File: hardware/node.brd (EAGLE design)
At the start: 16.5 x 25.6 mm, 48 parts, among them Q1 P-MOSFET, U1 ATMEGA32U4, U2 MCP1703CB/TOREX-XC6206, Y1 8MHz

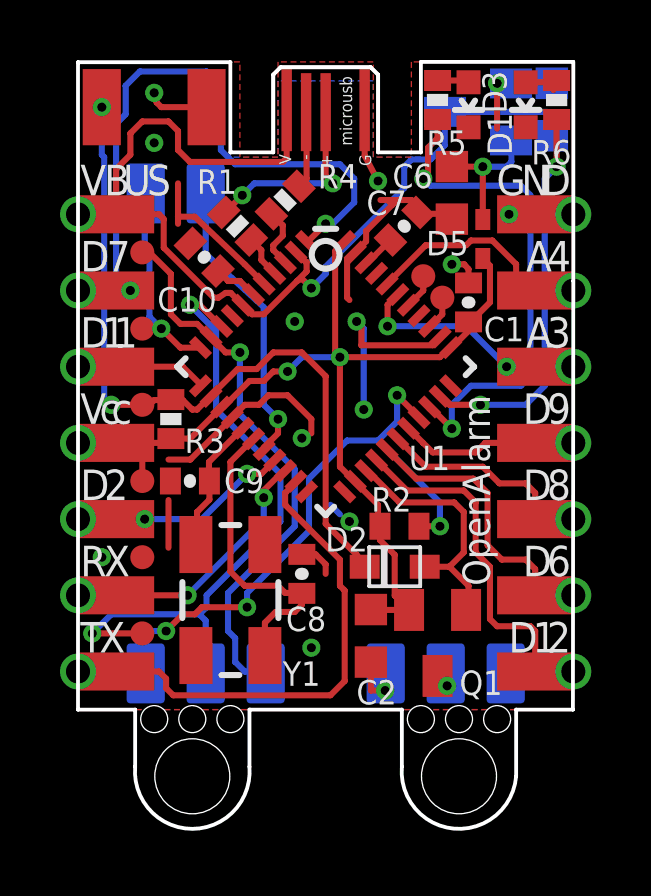
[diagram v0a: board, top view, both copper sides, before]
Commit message: Hardware update
Node 1.0.0, export and node shield
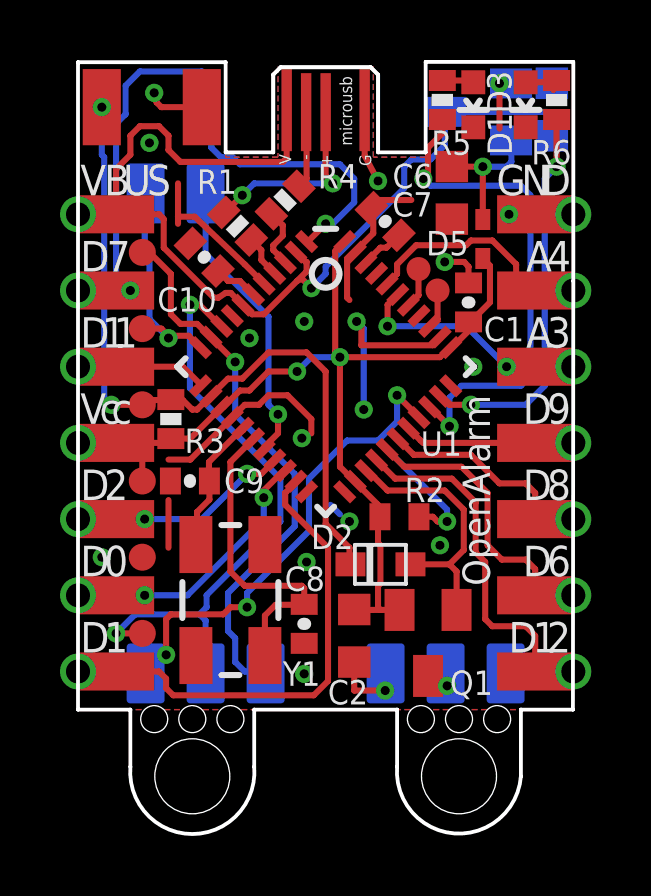
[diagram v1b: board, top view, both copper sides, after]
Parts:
- TP1, TP2, TP3, TP4, TP5, TP6: value TPTP08R -> TPTP09R; device testpad:TP08R -> testpad:TP09R
- moved C8 1.67 mm to (7.54, 2.86), turned to 270 degrees
- moved C7 0.65 mm to (10.2, 16.3), turned to 315 degrees
- moved C2 0.56 mm to (9.21, 2.46)
- moved D2 0.48 mm to (10.1, 4.84)
- moved Q1 0.32 mm to (11.7, 2.22)
- moved R2 0.32 mm to (10.7, 6.43)
- moved TP7 0.29 mm to (11.4, 14.7)
- moved TP8 0.29 mm to (12.0, 14.0)
- moved D3 0.16 mm to (13.2, 20.2)
- moved PAD8 0.16 mm to (4.13, 20.1)
- moved R5 0.16 mm to (12.1, 20.3)
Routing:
- net GND: track 40.2 -> 36.8 mm, vias 14 -> 18
- net SCK: track 21.6 -> 20.0 mm
- net RESET: track 26.1 -> 25.0 mm
- net TXO: track 16.0 -> 15.2 mm
- net VCC: track 32.2 -> 32.7 mm
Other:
- board size 16.5 x 25.6 mm -> 16.5 x 25.7 mm
- board text added: "0"
- board text added: "oa node v 1.x.x"
- board text removed: "R"
- board text removed: "T"
- board text removed: "X"
- board text removed: "oa node v 1.0.0"

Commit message: Before resize
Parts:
- added C3, C4: 1uF, SparkFun:0402-CAP
- added IC1: MAX1555, maxim:SOT23-5L
- added R7, R8: (no value), SparkFun:0402-RES
- added SV1: (no value), con-lsta:FE10
- added TP10, TP9: TPTP08R, testpad:TP08R
- C2: value 100nF -> 1uF; device rcl:C0603K -> SparkFun:0402-CAP
- C5: value 1uF -> 100nF; device rcl:C0603K -> SparkFun:0402-CAP
- C6: value 1u -> 1uF; device rcl:C0603K -> SparkFun:0402-CAP
- moved C5 19.0 mm to (9.53, 2.06), flipped to the top
- moved PAD2 17.3 mm to (15.2, 3.81)
- moved C2 17.1 mm to (1.91, 17.9), turned to 180 degrees
- moved PAD9 14.2 mm to (1.27, 14.0)
- moved PAD3 10.2 mm to (15.2, 11.4)
- moved C6 8.29 mm to (4.21, 17.9), turned to 0 degrees
- moved PAD5 2.54 mm to (15.2, 16.5)
- moved PAD6 2.54 mm to (15.2, 14.0)
- moved PAD13 2.54 mm to (1.27, 3.81)
- moved PAD14 2.54 mm to (1.27, 1.27)
- moved PAD4 2.54 mm to (15.2, 1.27)
- moved PAD10 2.54 mm to (1.27, 11.4)
- moved PAD7 2.54 mm to (1.27, 8.89)
- moved TP8 1.07 mm to (11.2, 14.7)
- moved TP7 0.79 mm to (12.0, 14.2)
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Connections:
- net D10 renamed D10_SEL
- net D13 renamed D13_LED_RED
- net D5 renamed D5_LED_GREEN
- net RXI renamed D0
- net TXO renamed D1
- removed net A0_NOTUSED: TP8.TP, U1.36
- removed net A1_NOTUSED: U1.37
- removed net A5_NOTUSED: U1.41
- removed net D11: PAD7.1, U1.12
- new net A0: PAD6.1, U1.36
- new net A1: PAD5.1, U1.37
- new net A5: TP10.TP, U1.41
- new net D11_IRQ: RFM12B1.IRQ, U1.12
- new net N$28: IC1.3
- new net N$9: C2.2, IC1.1
- net A3: now also TP8.TP; no longer PAD6.1
- net A4: now also R7.1, R8.2; no longer PAD5.1
- net D3: now also PAD7.1; no longer RFM12B1.IRQ
- net GND: now also C2.1, C3.1, C4.1, C5.1, C6.1, IC1.2, R8.1; no longer C2.2, C5.2, C6.2
- net N$11: now also C4.2; no longer C6.1
- net TXLED_NOTUSED: now also TP9.TP
- net VBUS: now also C3.2, R7.2; no longer C5.1
- net VCC: now also C5.2, C6.2, IC1.5; no longer C2.1
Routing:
- net VCC: track 32.7 -> 45.2 mm, vias 2 -> 6
- net A1: track 0.00 -> 7.72 mm, vias 0 -> 2
- net D1: track 15.2 -> 7.73 mm, vias 0 -> 2
- net D11_IRQ: track 0.00 -> 7.39 mm, vias 0 -> 1
- net A4: track 6.93 -> 0.01 mm
- net A3: track 6.68 -> 1.12 mm, vias 2 -> 0
- net VBUS: track 33.9 -> 29.5 mm, vias 1 -> 2
- net A0: track 0.00 -> 4.21 mm, vias 0 -> 2
- net D3: track 9.73 -> 6.26 mm, vias 1 -> 2
- net D11: track 3.10 -> 0.00 mm
- net D0: track 7.92 -> 11.0 mm
- net D6: track 8.49 -> 11.3 mm
- net N$9: track 0.00 -> 2.33 mm, vias 0 -> 1
- net D7: track 21.2 -> 19.1 mm
- net D10_SEL: track 20.5 -> 18.6 mm
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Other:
- board text added: "INT: D0, D1, D2, D3, D7"
- board text added: "PCINT: D8, D9"
- board text removed: "4"

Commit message: New node
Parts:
- moved R8 5.81 mm to (3.73, 18.1), flipped to the top
- moved R7 5.65 mm to (3.73, 17.1), flipped to the top, turned to 180 degrees
- moved SV1 4.84 mm to (35.3, 2.86)
- moved PAD1 2.54 mm to (17.8, 8.89)
- moved PAD11 2.54 mm to (17.8, 6.35)
- moved PAD2 2.54 mm to (17.8, 3.81)
- moved PAD3 2.54 mm to (17.8, 11.4)
- moved PAD4 2.54 mm to (17.8, 1.27)
- moved PAD5 2.54 mm to (17.8, 16.5)
- moved PAD6 2.54 mm to (17.8, 14.0)
- moved C2 2.53 mm to (0.56, 20.1), flipped to the bottom, turned to 270 degrees
- moved C6 2.49 mm to (5.48, 20.1), flipped to the bottom, turned to 270 degrees
- moved R6 2.38 mm to (18.3, 20.3)
- moved C3 2.25 mm to (18.0, 20.3)
- moved D1 2.22 mm to (17.1, 20.2)
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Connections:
- removed net N$9: C2.2, IC1.1
- net VBUS: now also C2.2, IC1.1
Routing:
- net GND: track 35.2 -> 24.7 mm, vias 21 -> 25
- net VBUS: track 29.5 -> 37.0 mm, vias 2 -> 3
- net VCC: track 45.2 -> 50.3 mm, vias 6 -> 4
- net N$9: track 2.33 -> 0.00 mm, vias 1 -> 0
- net A4: track 0.01 -> 2.21 mm
- net D6: track 11.3 -> 12.6 mm
- net A1: track 7.72 -> 9.01 mm
- net D9: track 4.43 -> 5.70 mm
- net D7: track 19.1 -> 20.4 mm
- net D3: track 6.26 -> 7.53 mm
- net D2: track 6.11 -> 7.38 mm
- net D1: track 7.73 -> 9.00 mm
- net A0: track 4.21 -> 5.48 mm
- net D8: track 6.34 -> 7.61 mm
- net RESET: track 26.0 -> 27.2 mm
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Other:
- board size 16.5 x 25.7 mm -> 19.1 x 25.7 mm

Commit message: Node
Avancement
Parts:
- added PAD17, PAD18, PAD19, PAD20, PAD21, PAD22, PAD23, PAD24, PAD25, PAD26, PAD27, PAD28, PAD29, PAD30, PAD31, PAD32, PAD33, PAD34, PAD35, PAD36, PAD37, PAD38, PAD39, PAD40, PAD41, PAD42, PAD43, PAD44, PAD45, PAD46, PAD47, PAD48, PAD49, PAD50, PAD51, PAD52, PAD53, PAD54, PAD55, PAD56, PAD57, PAD58: (no value), wirepad:SMD1,27-2,54
- added TP11: TPTP08R, testpad:TP08R
- moved SV1 21.5 mm to (29.8, 23.7)
- moved R3 0.78 mm to (4.13, 9.76)
- moved C10 0.50 mm to (5.56, 15.0)
- moved R1 0.50 mm to (6.91, 16.2)
- moved C1 0.32 mm to (14.8, 13.7)
- moved C4 0.32 mm to (14.2, 17.3)
- moved C5 0.32 mm to (11.1, 2.06)
- moved C7 0.32 mm to (11.5, 16.5)
- moved D3 0.32 mm to (15.2, 20.2)
- moved D5 0.32 mm to (15.9, 16.4)
- moved Q1 0.32 mm to (13.3, 2.22)
- moved TP10 0.32 mm to (12.8, 15.6)
- moved TP8 0.32 mm to (12.8, 14.7)
- moved IC1 0.32 mm to (3.33, 20.0)
- moved C6 0.32 mm to (5.79, 20.1)
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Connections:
- net TXLED_NOTUSED renamed TXLED
- removed net RXLED_NOTUSED: U1.8
- new net N$13: PAD33.1, PAD34.1
- new net N$27: PAD35.1, PAD36.1
- new net N$29: PAD37.1, PAD38.1
- new net N$30: PAD39.1, PAD40.1
- new net N$31: PAD41.1, PAD42.1
- new net N$32: PAD43.1, PAD44.1
- new net N$40: PAD45.1, PAD46.1
- new net N$41: PAD47.1, PAD48.1
- new net N$42: PAD49.1, PAD50.1
- new net N$43: PAD51.1, PAD52.1
- new net N$44: PAD53.1, PAD54.1
- new net N$45: PAD55.1, PAD56.1
- new net N$46: PAD57.1, PAD58.1
- new net N$9: PAD31.1, PAD32.1
- new net RXLED: TP11.TP, U1.8
- net A0: now also PAD29.1
- net A1: now also PAD30.1
- net D0: now also PAD23.1
- net D1: now also PAD22.1
- net D12: now also PAD28.1
- net D2: now also PAD21.1
- net D3: now also PAD20.1
- net D6: now also PAD24.1
- net D7: now also PAD25.1
- net D8: now also PAD26.1
- net D9: now also PAD27.1
- net GND: now also PAD18.1
- net VBUS: now also PAD17.1
- net VCC: now also PAD19.1
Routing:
- net GND: track 24.7 -> 80.1 mm, vias 25 -> 24
- net A4: track 2.21 -> 15.5 mm, vias 0 -> 2
- net VCC: track 50.3 -> 46.1 mm, vias 4 -> 2
- net D5_LED_GREEN: track 17.0 -> 13.2 mm
- net RXLED: track 0.00 -> 2.19 mm
- net D7: track 20.4 -> 19.6 mm
- net MOSI: track 19.9 -> 20.7 mm
- net D6: track 12.6 -> 13.2 mm
- net D+: track 6.94 -> 7.45 mm
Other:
- board size 19.1 x 25.7 mm -> 39.5 x 25.7 mm
- board text removed: "INT: D0, D1, D2, D3, D7"
- board text removed: "PCINT: D8, D9"

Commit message: Node
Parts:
- removed SV1: (no value), con-lsta:FE10
- added TP12: TPTP08R, testpad:TP08R
- D5: value (none) -> RB751S40
- moved C1 0.65 mm to (15.4, 13.6)
- moved R7 0.40 mm to (4.05, 16.7)
- moved R8 0.32 mm to (4.05, 17.8)
- moved TP7 0.29 mm to (13.7, 14.4)
- moved R4 0.29 mm to (8.65, 16.7)
- moved D5 0.18 mm to (15.7, 16.5)
- moved TP11 0.18 mm to (4.84, 13.6)
- moved PAD31 0.16 mm to (21.3, 16.5)
- moved PAD32 0.16 mm to (21.3, 16.5)
- moved PAD33 0.16 mm to (21.3, 14.0)
- moved PAD34 0.16 mm to (21.3, 14.0)
- moved PAD35 0.16 mm to (21.3, 11.4)
- moved PAD36 0.16 mm to (21.3, 11.4)
- moved PAD37 0.16 mm to (21.3, 8.89)
- moved PAD38 0.16 mm to (21.3, 8.89)
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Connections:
- net VBUS renamed VIN
- removed net N$28: IC1.3
- new net CHG: IC1.3, TP12.TP, U1.33
- net GND: no longer U1.33
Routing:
- net CHG: track 0.00 -> 21.4 mm, vias 0 -> 3
- net GND: track 80.1 -> 68.7 mm, vias 24 -> 25
- net VCC: track 46.1 -> 51.3 mm, vias 2 -> 3
- net A4: track 15.5 -> 13.8 mm
- net D7: track 19.6 -> 18.1 mm, vias 2 -> 1
- net D0: track 11.6 -> 12.7 mm, vias 2 -> 1
- net VIN: track 36.6 -> 35.7 mm
- net D12: track 10.5 -> 11.4 mm, vias 2 -> 1
- net RESET: track 27.1 -> 27.6 mm
- net D3: track 7.84 -> 8.32 mm, vias 2 -> 1
- net D+: track 7.45 -> 7.82 mm, vias 2 -> 0
- net A0: track 5.48 -> 5.69 mm, vias 2 -> 1
- net D13_LED_RED: track 13.6 -> 13.8 mm, vias 2 -> 4
- net A1: track 9.01 -> 8.92 mm, vias 2 -> 1
- net D2: vias 2 -> 1
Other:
- board size 39.5 x 25.7 mm -> 39.4 x 25.7 mm
- board text added: "C"
- board text added: "I"
- board text removed: "B"
- board text removed: "S"
- board text removed: "U"
- board text removed: "c"

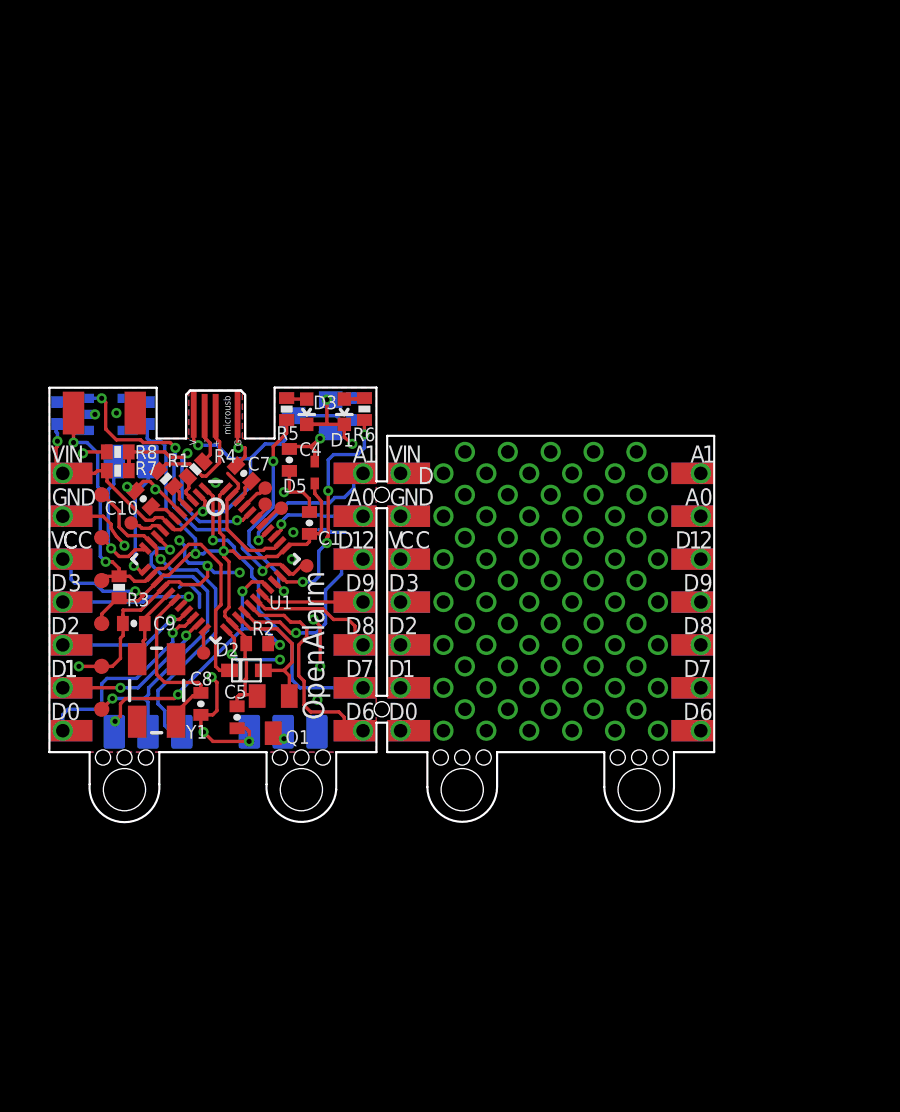
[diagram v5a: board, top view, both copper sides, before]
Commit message: Max1555 backup
Finally, design with max1555 is a bad idea !
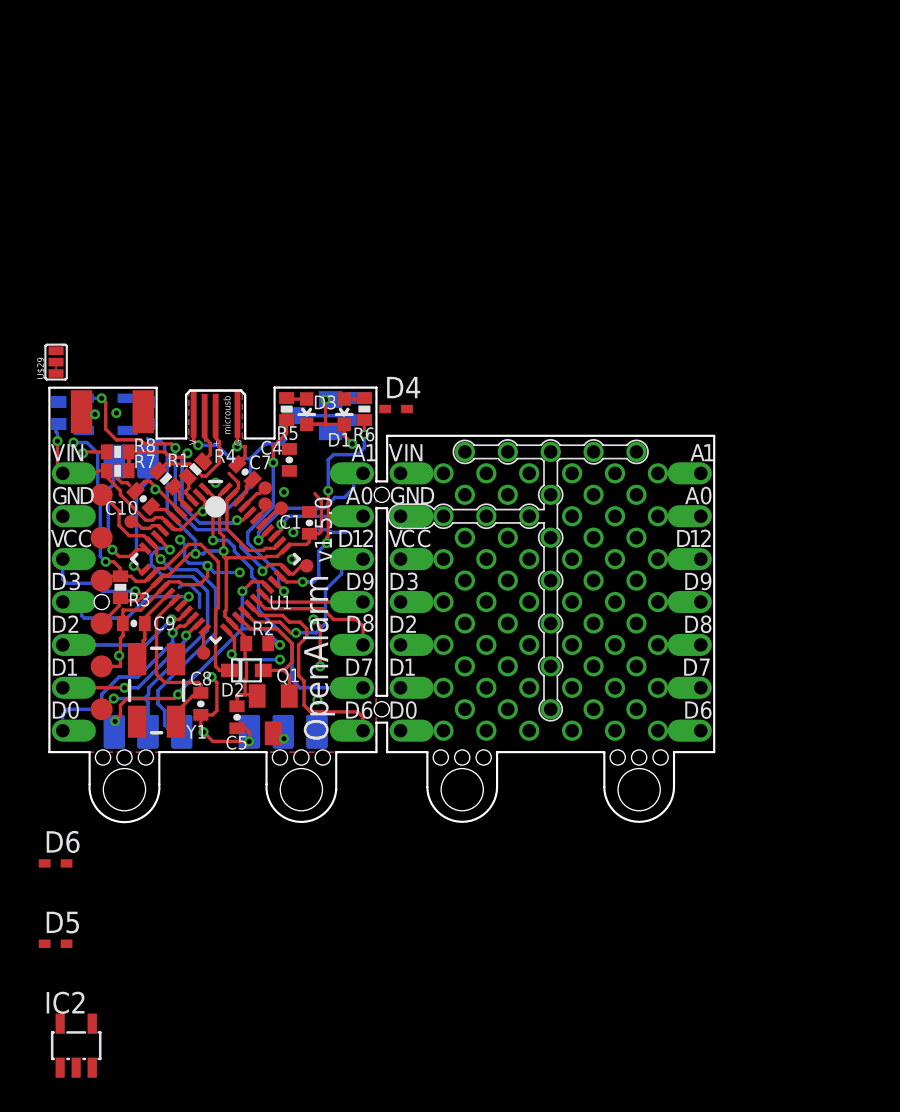
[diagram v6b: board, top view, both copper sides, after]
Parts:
- removed PAD1, PAD10, PAD11, PAD12, PAD13, PAD14, PAD15, PAD17, PAD18, PAD19, PAD2, PAD20, PAD21, PAD22, PAD23, PAD24, PAD25, PAD26, PAD27, PAD28, PAD29, PAD3, PAD30, PAD31, PAD32, PAD33, PAD34, PAD35, PAD36, PAD37, PAD38, PAD39, PAD4, PAD40, PAD41, PAD42, PAD43, PAD44, PAD45, PAD46, PAD47, PAD48, PAD49, PAD5, PAD50, PAD51, PAD52, PAD53, PAD54, PAD55, PAD56, PAD57, PAD58, PAD6, PAD7, PAD9: (no value), wirepad:SMD1,27-2,54
- removed PAD16: RESET1, wirepad:SMD1,27-2,54
- removed PAD8: RESET0, wirepad:SMD1,27-2,54
- removed TP6: TPTP09R, testpad:TP09R
- added D4, D6: RB751S40, diode:SOD523
- added IC2: TS5205, v-reg:SOT25
- added RESET: MICROSWITCH, openalarm:MICROSWITCH
- added TP14: TPTP13R, testpad:TP13R
- added U$1, U$10, U$11, U$12, U$13, U$14, U$15, U$16, U$17, U$18, U$19, U$2, U$20, U$21, U$22, U$23, U$24, U$25, U$26, U$27, U$28, U$3, U$4, U$5, U$6, U$7, U$8, U$9: IOPAD, openalarm:IOPAD
- added U$29: UJUMPER-SHORT, openalarm:UJUMPER-SHORT
- TP1, TP2, TP3, TP4, TP5: value TPTP09R -> TPTP13R; device testpad:TP09R -> testpad:TP13R
- moved D5 31.8 mm to (0.32, -11.4), turned to 0 degrees
- moved TP5 10.2 mm to (3.10, 5.08)
- moved TP4 7.62 mm to (3.10, 15.2)
- moved TP1 5.08 mm to (3.10, 7.62)
- moved C7 0.11 mm to (11.6, 16.6)
- moved TP11 0.08 mm to (4.84, 13.7)
- moved R3 0.08 mm to (4.21, 9.76)
- renumbered RFM12B1 to RFMXX
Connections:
- removed net VIN: C2.2, C3.2, IC1.1, JP1.1, PAD15.1, PAD17.1, R7.2, U1.2, U1.7, U2.3
- new net N$12: C6.2, D5.A, D6.C
- new net N$14: IC1.4, U$29.C0
- new net N$15: C2.2, U$29.COM
- new net N$16: D6.A, IC1.5
- new net VBAT: C4.2, D4.A, U2.2
- new net VBUS: C3.2, JP1.1, R7.2, U$7.P$2, U1.2, U1.7, U2.3
- net A0: now also U$9.P$2; no longer PAD29.1, PAD6.1
- net A1: now also U$8.P$2; no longer PAD30.1, PAD5.1
- net D0: now also U$2.P$2; no longer PAD14.1, PAD23.1
- net D1: now also U$1.P$2; no longer PAD13.1, PAD22.1
- net D12: now also U$10.P$2; no longer PAD28.1, PAD3.1
- net D2: now also U$3.P$2; no longer PAD12.1, PAD21.1
- net D3: now also U$4.P$2; no longer PAD20.1, PAD7.1
- net D6: now also U$14.P$2; no longer PAD24.1, PAD4.1
- net D7: now also U$13.P$2; no longer PAD2.1, PAD25.1
- net D8: now also U$12.P$2; no longer PAD11.1, PAD26.1
- net D9: now also U$11.P$2; no longer PAD1.1, PAD27.1
- net GND: now also RESET.P$1, TP5.TP, U$6.P$2; no longer PAD18.1, PAD8.1, PAD9.1, TP6.TP
- net MISO: now also TP14.TP; no longer TP1.TP
- net MOSI: now also TP4.TP; no longer TP5.TP
- net N$11: now also IC1.1, U$29.C1; no longer C4.2, D5.A, U2.2
- net N$13: now also U$16.P$2; no longer PAD33.1, PAD34.1
- net N$27: now also U$17.P$2; no longer PAD35.1, PAD36.1
- net N$29: now also U$18.P$2; no longer PAD37.1, PAD38.1
- net N$30: now also U$19.P$2; no longer PAD39.1, PAD40.1
- net N$31: now also U$20.P$2; no longer PAD41.1, PAD42.1
- net N$32: now also U$21.P$2; no longer PAD43.1, PAD44.1
- net N$40: now also U$23.P$2; no longer PAD45.1, PAD46.1
- net N$41: now also U$24.P$2; no longer PAD47.1, PAD48.1
- net N$42: now also U$25.P$2; no longer PAD49.1, PAD50.1
- net N$43: now also U$26.P$2; no longer PAD51.1, PAD52.1
- net N$44: now also U$27.P$2; no longer PAD53.1, PAD54.1
- net N$45: now also U$28.P$2; no longer PAD55.1, PAD56.1
- net N$46: now also U$22.P$2; no longer PAD57.1, PAD58.1
- net N$9: now also U$15.P$2; no longer PAD31.1, PAD32.1
- net RESET: now also RESET.P$2; no longer PAD16.1
- net VCC: now also D4.C, TP1.TP, U$5.P$2; no longer C6.2, D5.C, IC1.5, PAD10.1, PAD19.1, TP4.TP
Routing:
- net VIN: track 35.7 -> 0.00 mm, vias 3 -> 0
- net VBUS: track 0.00 -> 33.6 mm, vias 0 -> 3
- net GND: track 68.7 -> 61.0 mm, vias 25 -> 23
- net N$11: track 4.44 -> 0.00 mm, vias 1 -> 0
- net VCC: track 51.3 -> 48.5 mm
- net RESET: track 27.6 -> 25.5 mm
- net D3: track 8.32 -> 9.43 mm
- net D0: track 12.7 -> 11.7 mm
- net A1: track 8.92 -> 9.44 mm
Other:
- board text added: "oa node"
- board text added: "v1.5.0"
- board text removed: "oa node v 1.x.x"
